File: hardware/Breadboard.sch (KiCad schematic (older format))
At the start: 38 parts, among them J1 8PinBeardboard, U5 PCF8574, U6 ULN2003, U7 PCF8574, U8 A4988 Module, U9 MCP23017_SP

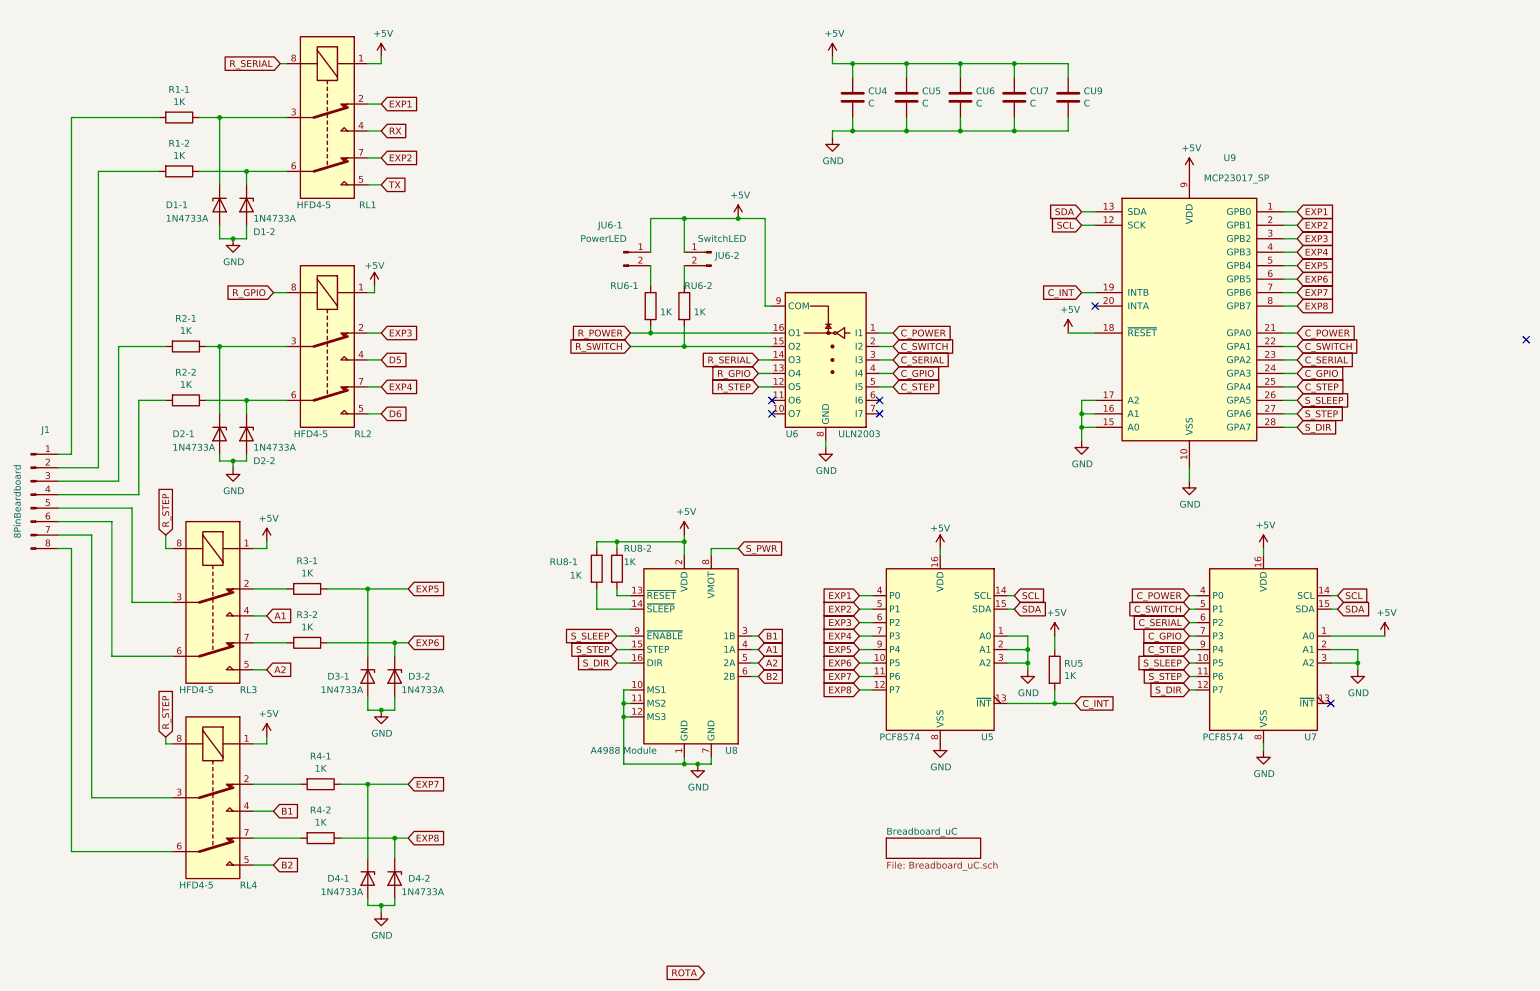
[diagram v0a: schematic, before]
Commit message: Bugfixes, prepare for 4066
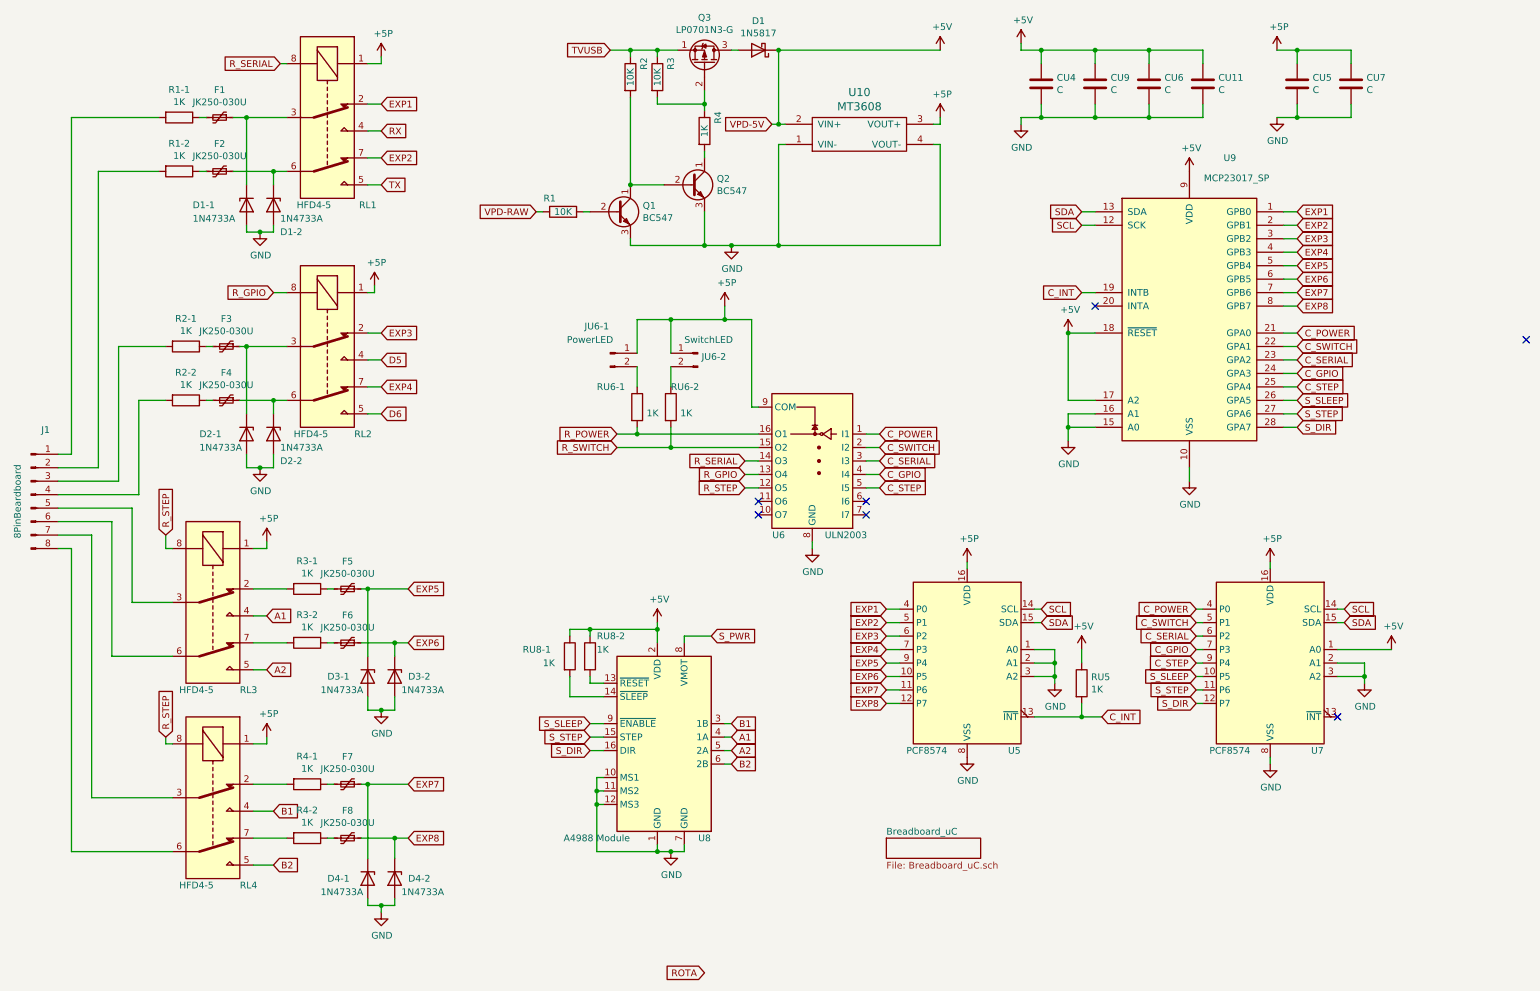
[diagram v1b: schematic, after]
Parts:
- added CU11: C, Capacitor_THT:C_Axial_L3.8mm_D2.6mm_P7.50mm_Horizontal, symbol Device:C
- added D1: 1N5817, Diode_THT:D_DO-41_SOD81_P10.16mm_Horizontal, symbol Diode:1N5817
- added F1, F2, F3, F4, F5, F6, F7, F8: JK250-030U, Fuse:Fuse_BelFuse_0ZRE0005FF_L8.3mm_W3.8mm, symbol Device:Polyfuse_Small
- added Q1, Q2: BC547, Package_TO_SOT_THT:TO-92_Inline, symbol Transistor_BJT:BC547
- added Q3: LP0701N3-G, Package_TO_SOT_THT:TO-92L_Inline, symbol Device:Q_PMOS_SGD
- added R1, R2, R3: 10K, Resistor_THT:R_Axial_DIN0204_L3.6mm_D1.6mm_P7.62mm_Horizontal, symbol Device:R
- added R4: 1K, Resistor_THT:R_Axial_DIN0204_L3.6mm_D1.6mm_P7.62mm_Horizontal, symbol Device:R
- added U10: MT3608, Custom:dcdc-booster-board, symbol symbols:dcdc-booster-board
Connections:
- net +5V: now also U9.17 (A2), CU11.1, D1.1 (K), U10.2 (VIN+); no longer CU5.1, CU7.1, JU6-1.1 (Pin_1), JU6-2.1 (Pin_1), RL1.1, RL2.1, RL3.1, RL4.1, U5.16 (VDD), U6.9 (COM), U7.16 (VDD)
- net EXP5: now also F5.1; no longer R3-1.1
- net EXP6: now also F6.1; no longer R3-2.1
- net EXP7: now also F7.1; no longer R4-1.1
- net EXP8: now also F8.1; no longer R4-2.1
- net GND: now also CU11.2, Q1.3 (E), Q2.3 (E), U10.1 (VIN-), U10.4 (VOUT-); no longer U9.17 (A2)
- net at D1-1.1 (K), RL1.3: now also F1.1; no longer R1-1.1
- net at D1-2.1 (K), RL1.6: now also F2.1; no longer R1-2.1
- net at D2-1.1 (K), RL2.3: now also F3.1; no longer R2-1.1
- net at D2-2.1 (K), RL2.6: now also F4.1; no longer R2-2.1
- new net: F1.2, R1-1.1
- new net: F2.2, R1-2.1
- new net: F3.2, R2-1.1
- new net: F4.2, R2-2.1
- new net: F5.2, R3-1.1
- new net: F6.2, R3-2.1
- new net: F7.2, R4-1.1
- new net: F8.2, R4-2.1
- new net: Q3.2 (G), R3.2, R4.1
- new net: D1.2 (A), Q3.3 (D)
- new net: Q2.1 (C), R4.2
- new net: Q1.1 (C), Q2.2 (B), R2.2
- new net: Q1.2 (B), R1.2
- new net +5P: CU5.1, CU7.1, JU6-1.1 (Pin_1), JU6-2.1 (Pin_1), RL1.1, RL2.1, RL3.1, RL4.1, U10.3 (VOUT+), U5.16 (VDD), U6.9 (COM), U7.16 (VDD)
- new net TVUSB: Q3.1 (S), R2.1, R3.1
- new net VPD-RAW: R1.1
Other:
- moved on the sheet: CU4, CU5, CU6, CU7, CU9, D1-1, D1-2, D2-1, D2-2, JU6-1, JU6-2, R4-1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

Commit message: bugfixes & 4066 functionality
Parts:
- removed CU11: C, Capacitor_THT:C_Axial_L3.8mm_D2.6mm_P7.50mm_Horizontal, symbol Device:C
- added R17: 100, Resistor_THT:R_Axial_DIN0204_L3.6mm_D1.6mm_P7.62mm_Horizontal, symbol Device:R
- C1: renamed from CU4; value C -> 100pF
- C2: renamed from CU9; value C -> 100pF
- C3: renamed from CU6; value C -> 100pF
- C4: renamed from CU5; value C -> 100pF
- C5: renamed from CU7; value C -> 100pF
- F1, F2, F3, F4, F5, F6, F7, F8: value JK250-030U -> POLYF
- J1: value 8PinBeardboard -> MP1-8
- J2: renamed from JU6-1; value PowerLED -> PWRLED
- J3: renamed from JU6-2; value SwitchLED -> SWLED
- Q3: footprint Package_TO_SOT_THT:TO-92L_Inline -> Package_TO_SOT_THT:TO-92_Inline
- RL1: renamed from RL3; value HFD4-5 -> HFD4
- RL2: renamed from RL4; value HFD4-5 -> HFD4
- RL3: renamed from RL1; value HFD4-5 -> HFD4
- RL4: renamed from RL2; value HFD4-5 -> HFD4
- U1: renamed from U8; value A4988 Module -> A4988
- U5: renamed from U9; value MCP23017_SP -> MCP23017
- renumbered D1-1 to D1, D2-1 to D2, D1-2 to D3, D2-2 to D4, D3-1 to D5, D4-1 to D6, D3-2 to D7, D4-2 to D8, D1 to D9, R1-1 to R1, R1 to R10, RU8-2 to R11, R2 to R12, RU6-1 to R13, R3 to R14, RU6-2 to R15, R4 to R16, RU5 to R18, R1-2 to R2, R2-1 to R3, R2-2 to R4, R3-1 to R5, R3-2 to R6, R4-1 to R7, R4-2 to R8, RU8-1 to R9, U6 to U2, U10 to U3, U5 to U4, U7 to U6
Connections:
- net +5P: now also C1.1, C2.1, C3.1, U5.9 (VDD); no longer C4.1, C5.1
- net +5V: now also C4.1, C5.1; no longer C1.1, C2.1, C3.1, U5.9 (VDD)
- net C_INT: now also R17.2; no longer U5.19 (INTB)
- new net: R17.1, U5.19 (INTB)
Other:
- moved on the sheet: C4, C5, R11, R9, U1, U5

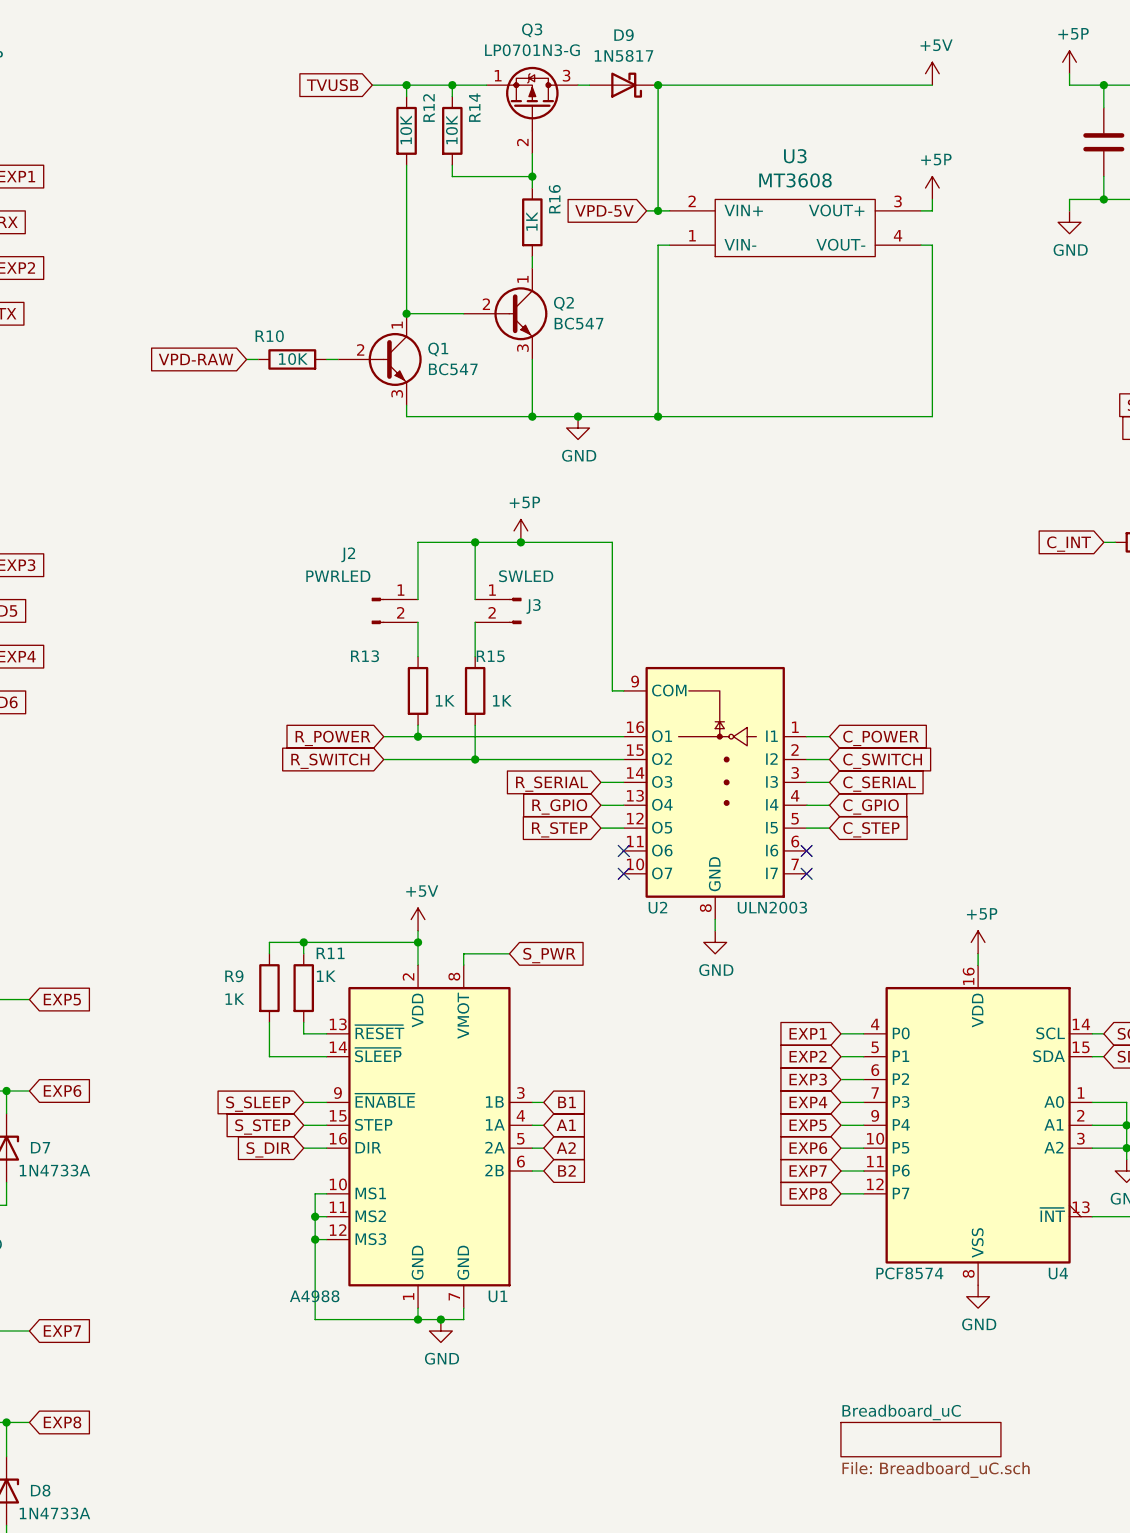
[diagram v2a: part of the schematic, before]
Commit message: Updated SPI protocol
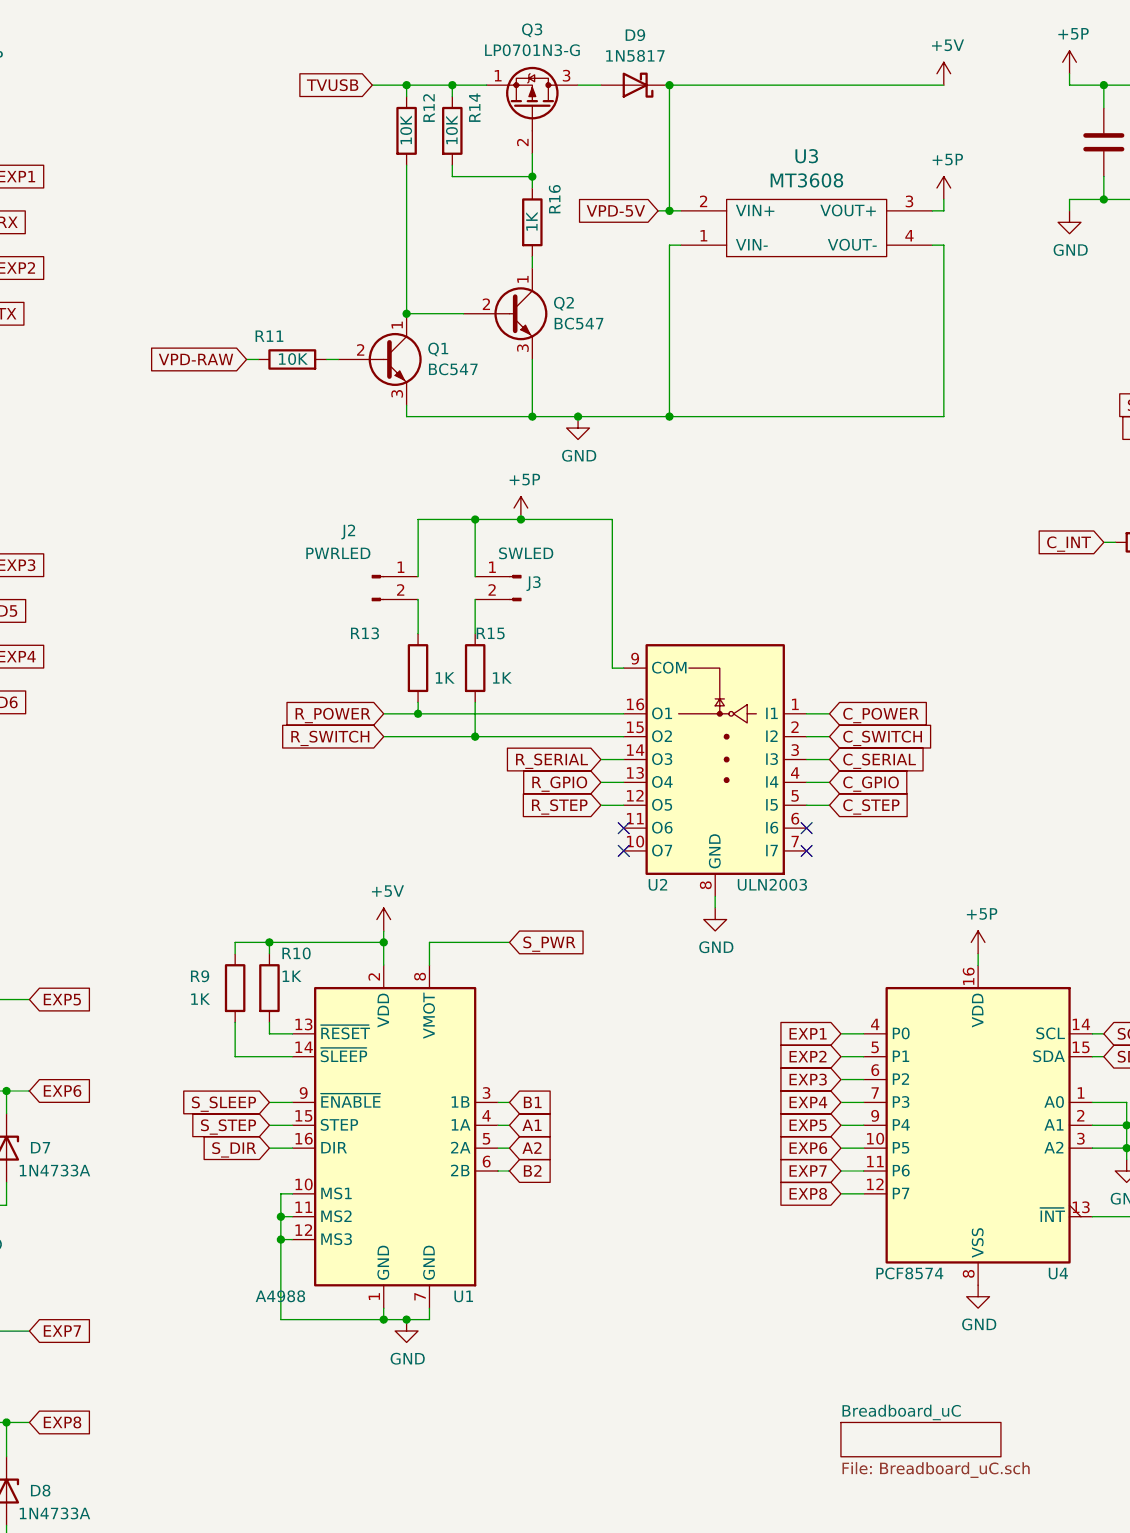
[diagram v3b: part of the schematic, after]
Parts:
- renumbered R11 to R10, R10 to R11
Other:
- moved on the sheet: D9, J2, J3, R10, R13, R15, R9, U1, U2, U3
